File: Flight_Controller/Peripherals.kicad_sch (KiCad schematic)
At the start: 44 parts, among them IC1 AT7456E, U2 BMI270, U3 TLV75533PDBV, U4 W25Q128JVSIQ TR, U6 LMR51625XDDCR, Y2 ABM3-27.000MHZ-D2Y-T

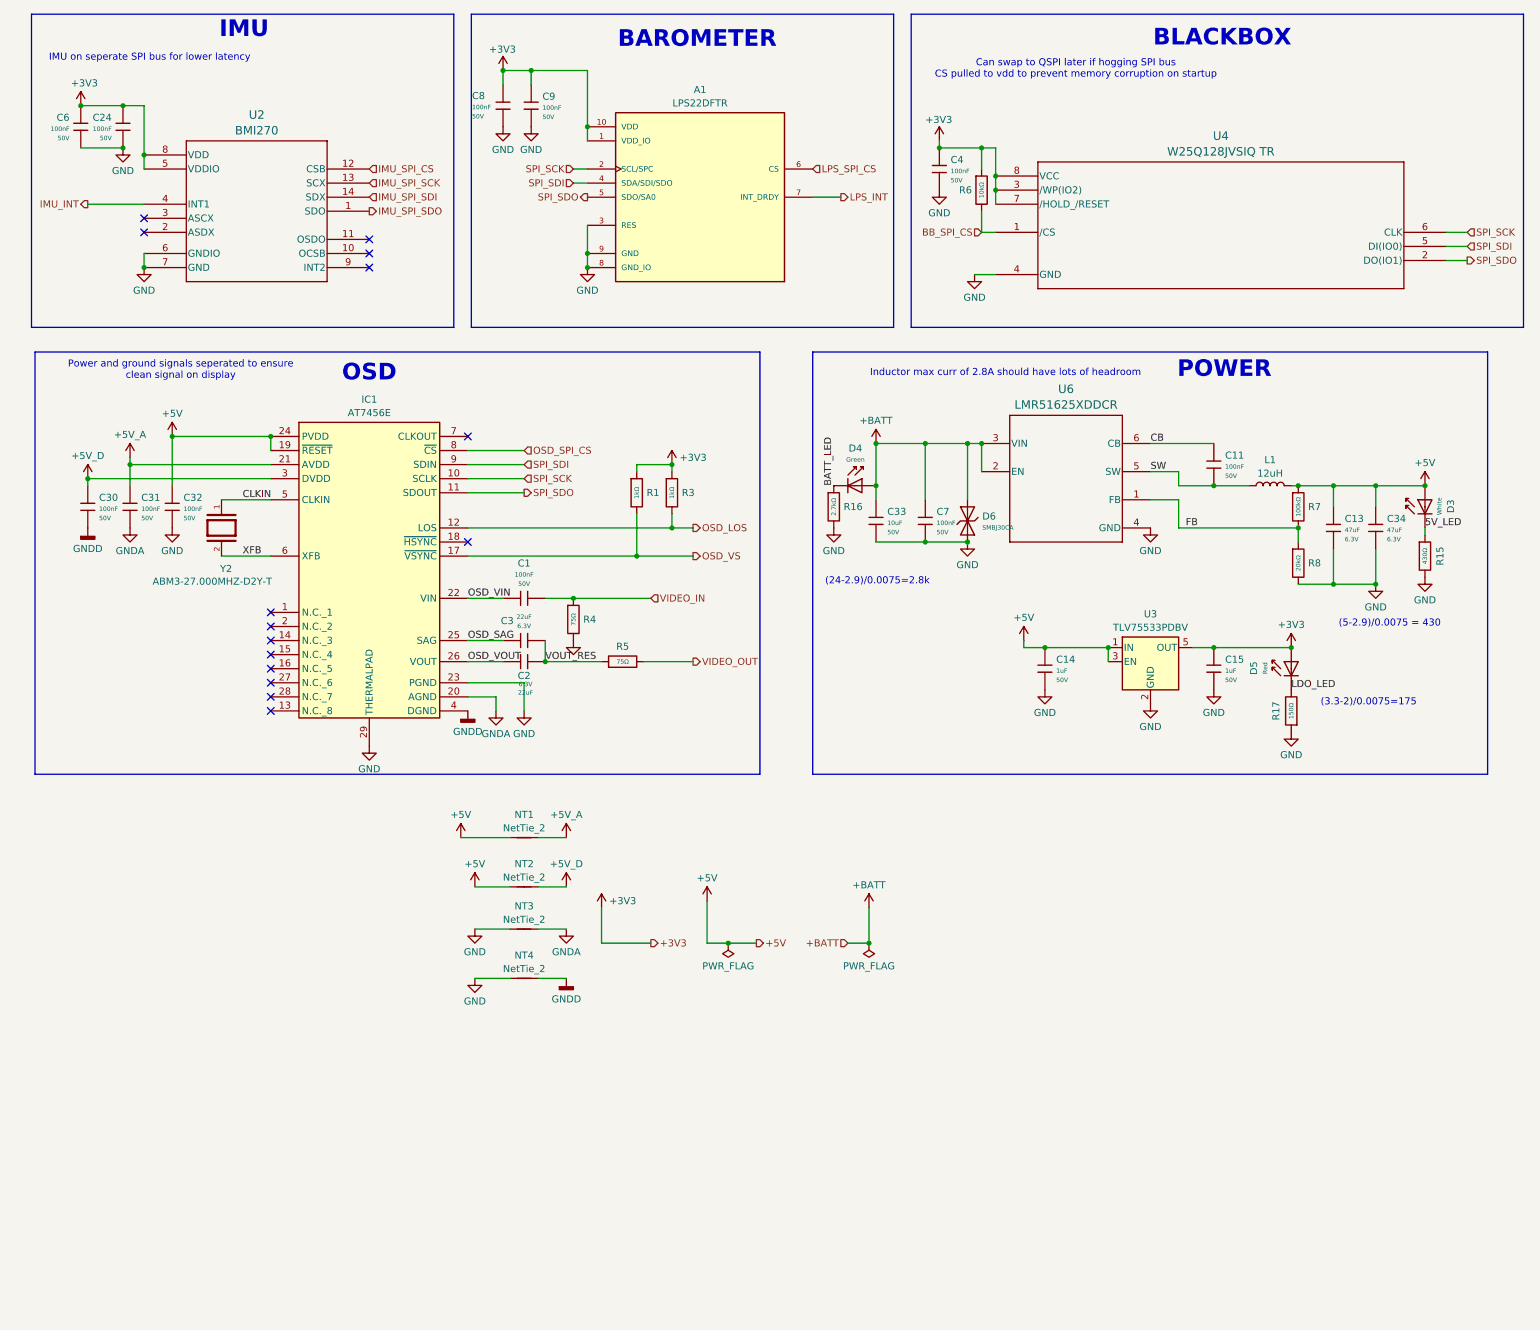
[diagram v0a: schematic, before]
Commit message: Added 9V Buck, GPS + Mag, Digital VTX
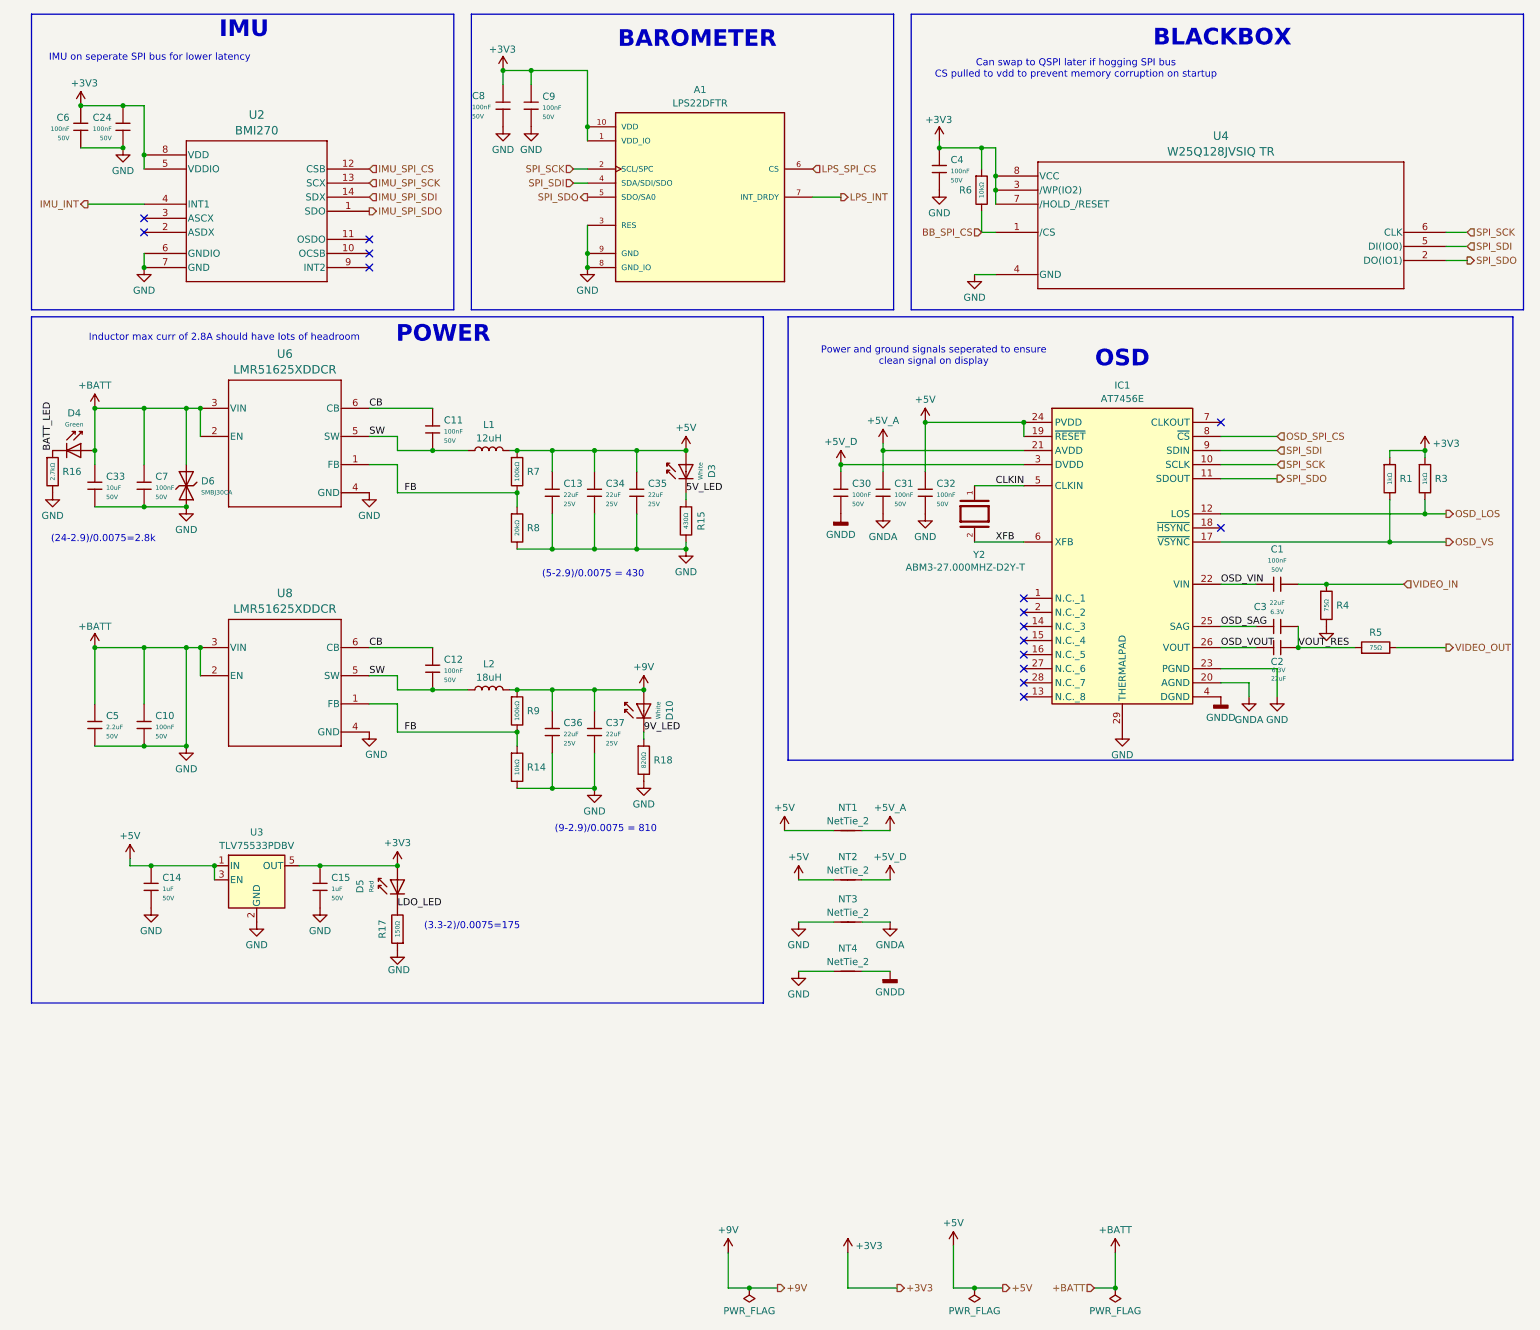
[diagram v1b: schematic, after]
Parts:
- removed C13, C34: 47uF, PCM_JLCPCB:C_0805, symbol PCM_JLCPCB-Capacitors:0805,47uF
- added C10, C12: 100nF, PCM_JLCPCB:C_0603, symbol PCM_JLCPCB-Capacitors:0603,100nF
- added C13, C34, C35, C36, C37: 22uF, PCM_JLCPCB:C_1206, symbol PCM_JLCPCB-Capacitors:1206,22uF,(2)
- added C5: 2.2uF, PCM_JLCPCB:C_0805, symbol PCM_JLCPCB-Capacitors:0805,2.2uF
- added D10: White, PCM_JLCPCB:D_0603, symbol PCM_JLCPCB-Diodes:LED,0603,White
- added L2: 18uH, Inductor_SMD:L_TDK_VLS6045EX_VLS6045AF, symbol Device:L
- added R14: 10kΩ, PCM_JLCPCB:R_0603, symbol PCM_JLCPCB-Resistors:0603,10kΩ
- added R18: 820Ω, PCM_JLCPCB:R_0603, symbol PCM_JLCPCB-Resistors:0603,820Ω
- added R9: 100kΩ, PCM_JLCPCB:R_0603, symbol PCM_JLCPCB-Resistors:0603,100kΩ
- added U8: LMR51625XDDCR, Flight_Controller:DDC0006A-MFG, symbol Flight_Controller:LMR51625XDDCR
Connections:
- net GND is gone; now on net +BATT: A1.3 (RES), A1.8 (GND_IO), A1.9 (GND), C14.2, C15.2, C24.2, C32.2, C33.2, C4.2, C6.2, C7.2, C8.2, C9.2, D6.1, IC1.23 (PGND), IC1.29 (THERMALPAD), NT3.2, NT4.2, R15.2, R16.2, R17.1, R4.2, R8.2, U2.6 (GNDIO), U2.7 (GND), U3.2 (GND), U4.4 (GND), U6.4 (GND)
- net +5V: now also C13.1, C34.1, C35.1
- net +BATT: now also C10.1, C10.2, C13.2, C34.2, C35.2, C36.2, C37.2, C5.1, C5.2, R14.2, R18.2, U8.2 (EN), U8.3 (VIN), U8.4 (GND)
- net CB: now also C12.1, U8.6 (CB)
- net FB: now also R14.1, R9.2, U8.1 (FB)
- net SW: now also C12.2, L2.1, U8.5 (SW)
- new net +9V: C36.1, C37.1, D10.2, L2.2, R9.1
- new net 9V_LED: D10.1, R18.1
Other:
- note added: "(9-2.9)/0.0075 = 810"
- moved on the sheet: C1, C11, C14, C15, C2, C3, C30, C31, C32, C33, C7, D3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

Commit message: Updated Footprints
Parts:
- L2: footprint Inductor_SMD:L_TDK_VLS6045EX_VLS6045AF -> Inductor_SMD:L_TDK_VLP8040
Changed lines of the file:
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@@
 	)
 	(junction
+		(at 247.65 120.65)
+		(diameter 0)
+		(color 0 0 0 0)
+	)
+	(junction
 		(at 30.48 34.29)
 		(diameter 0)
@@
 	)
 	(junction
-		(at 247.65 120.65)
-		(diameter 0)
-		(color 0 0 0 0)
-	)
-	(junction
 		(at 30.48 41.91)
 		(diameter 0)
@@
 	(wire
 		(pts
+			(xy 247.65 120.65) (xy 261.62 120.65)
+		)
+		(stroke
+			(width 0)
+			(type default)
+		)
+	)
+	(wire
+		(pts
 			(xy 99.06 27.94) (xy 99.06 30.48)
 		)
@@
 	(wire
 		(pts
-			(xy 247.65 120.65) (xy 261.62 120.65)
-		)
-		(stroke
-			(width 0)
-			(type default)
-		)
-	)
-	(wire
-		(pts
 			(xy 265.43 97.79) (xy 265.43 96.52)
 		)
@@
 		)
 	)
-	(label ""
-		(at 257.81 120.65 0)
-		(effects
-			(font
-				(size 1.27 1.27)
-			)
-			(justify left bottom)
-		)
-	)
 	(label "BATT_LED"
 		(at 17.78 96.52 90)
@@
 			)
 		)
-		(property "Footprint" "Inductor_SMD:L_TDK_VLS6045EX_VLS6045AF"
+		(property "Footprint" "Inductor_SMD:L_TDK_VLP8040"
 			(at 96.52 139.7 0)
 			(hide yes)

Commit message: Updated Layout to 60x30
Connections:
- net +BATT: no longer A1.3 (RES), A1.8 (GND_IO), A1.9 (GND), C10.2, C13.2, C14.2, C15.2, C24.2, C32.2, C33.2, C34.2, C35.2, C36.2, C37.2, C4.2, C5.2, C6.2, C7.2, C8.2, C9.2, D6.1, IC1.23 (PGND), IC1.29 (THERMALPAD), NT3.2, NT4.2, R14.2, R15.2, R16.2, R17.1, R18.2, R4.2, R8.2, U2.6 (GNDIO), U2.7 (GND), U3.2 (GND), U4.4 (GND), U6.4 (GND), U8.4 (GND)
- net CB renamed CB_5V
- net CB_5V: no longer C12.1, U8.6 (CB)
- net FB renamed FB_5V
- net FB_5V: no longer R14.1, R9.2, U8.1 (FB)
- net SW renamed SW_5V
- net SW_5V: no longer C12.2, L2.1, U8.5 (SW)
- new net CB_9V: C12.1, U8.6 (CB)
- new net FB_9V: R14.1, R9.2, U8.1 (FB)
- new net GND: A1.3 (RES), A1.8 (GND_IO), A1.9 (GND), C10.2, C13.2, C14.2, C15.2, C24.2, C32.2, C33.2, C34.2, C35.2, C36.2, C37.2, C4.2, C5.2, C6.2, C7.2, C8.2, C9.2, D6.1, IC1.23 (PGND), IC1.29 (THERMALPAD), NT3.2, NT4.2, R14.2, R15.2, R16.2, R17.1, R18.2, R4.2, R8.2, U2.6 (GNDIO), U2.7 (GND), U3.2 (GND), U4.4 (GND), U6.4 (GND), U8.4 (GND)
- new net SW_9V: C12.2, L2.1, U8.5 (SW)
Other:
- moved on the sheet: R17
